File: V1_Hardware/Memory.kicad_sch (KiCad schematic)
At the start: 6 parts, among them J4 1040310811, U9 W25Q128JVE

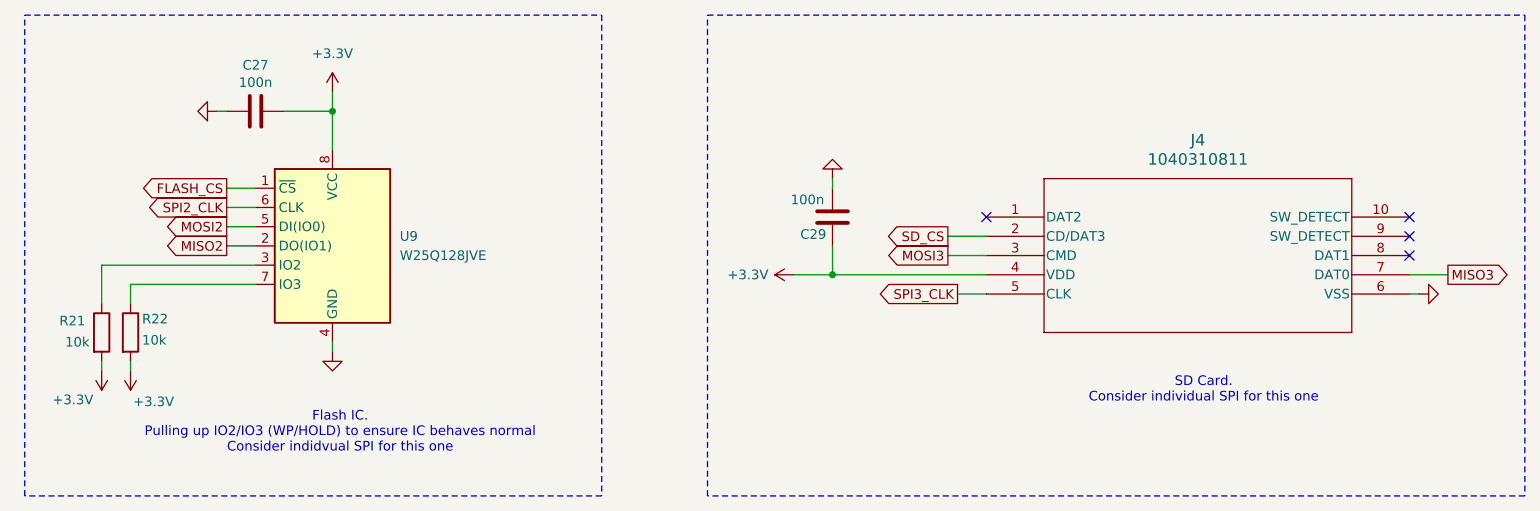
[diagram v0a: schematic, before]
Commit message: added the V1 to personal repo from org repo
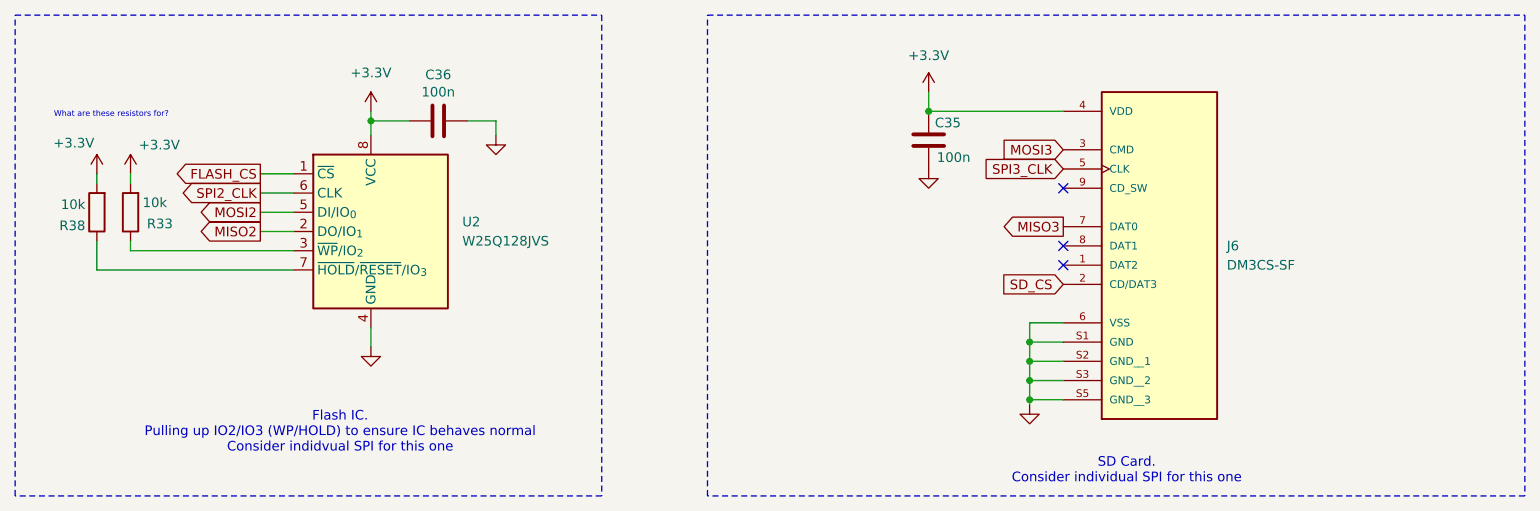
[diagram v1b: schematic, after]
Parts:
- removed C27, C29: 100n, symbol Device:C
- removed J4: 1040310811, 104031-0811_MOL, symbol 1040310811:1040310811
- removed R21, R22: 10k, symbol Device:R
- removed U9: W25Q128JVE, Package_SON:WSON-8-1EP_8x6mm_P1.27mm_EP3.4x4.3mm, symbol Memory_Flash:W25Q128JVE
- added C35, C36: 100n, Capacitor_SMD:C_0603_1608Metric_Pad1.08x0.95mm_HandSolder, symbol Device:C
- added J6: DM3CS-SF, V1:DM3CS-SF, symbol DM3CS-SF:DM3CS-SF
- added R33, R38: 10k, Resistor_SMD:R_0603_1608Metric_Pad0.98x0.95mm_HandSolder, symbol Device:R
- added U2: W25Q128JVS, Package_SO:SOIC-8_5.3x5.3mm_P1.27mm, symbol Memory_Flash:W25Q128JVS
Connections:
- net +3.3V: now also C35.2, C36.1, J6.4 (VDD), R33.2, R38.2, U2.8 (VCC)
- net FLASH_CS: now also U2.1 (~{CS})
- net GND: now also C35.1, C36.2, J6.6 (VSS), J6.S1 (GND), J6.S2 (GND__1), J6.S3 (GND__2), J6.S5 (GND__3), U2.4 (GND)
- net MISO2: now also U2.2 (DO/IO_{1})
- net MISO3: now also J6.7 (DAT0)
- net MOSI2: now also U2.5 (DI/IO_{0})
- net MOSI3: now also J6.3 (CMD)
- net SD_CS: now also J6.2 (CD/DAT3)
- net SPI2_CLK: now also U2.6 (CLK)
- net SPI3_CLK: now also J6.5 (CLK)
- new net: R33.1, U2.3 (~{WP}/IO_{2})
- new net: R38.1, U2.7 (~{HOLD}/~{RESET}/IO_{3})
- no-connect marks 4 -> 3
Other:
- note added: "What are these resistors for?"
